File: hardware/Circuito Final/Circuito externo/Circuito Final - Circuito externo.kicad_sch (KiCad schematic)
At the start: 81 parts, among them J1 Conn_02x19_Odd_Even, J2 Conn_02x19_Odd_Even, J3 Conn_01x02, J4 Conn_01x02, J5 Conn_01x03_Pin, Q1 FDMS6681Z, Q2 FDMS6681Z, Q3 MMBT2222A, SW1 SW_SPDT, SW2 SW_DIP_x04, SW3 SW_DIP_x04, SW4 SW_DIP_x01, SW5 SW_DIP_x01, SW6 SW_DIP_x01, U1 Opamp_Quad, U2 ICL7660, U3 INA180A1, U4 INA180A1

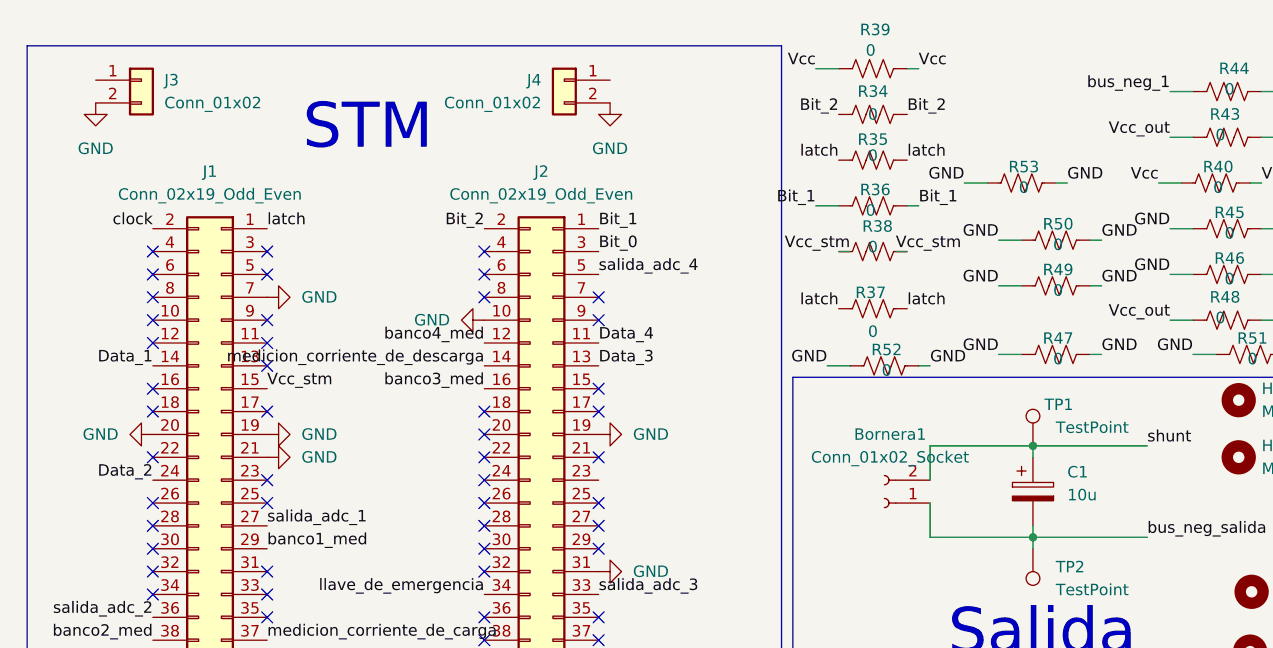
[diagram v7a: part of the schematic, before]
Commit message: sube placa con los oines arreglados
estaba mal data 2, data 1, y vcc
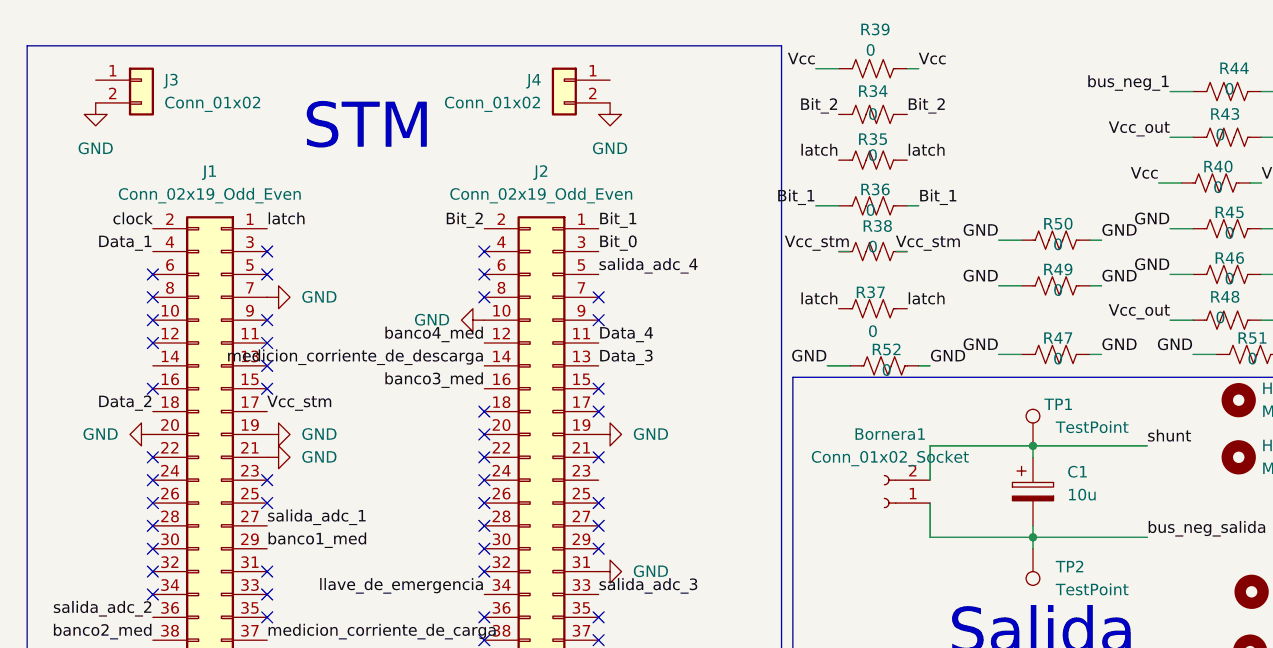
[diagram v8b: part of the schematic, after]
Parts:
- removed R53: 0, Resistor_SMD:R_1206_3216Metric_Pad1.30x1.75mm_HandSolder, symbol Device:R_US
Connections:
- net Data_1: now also J1.4 (Pin_4); no longer J1.14 (Pin_14)
- net Data_2: now also J1.18 (Pin_18); no longer J1.24 (Pin_24)
- net Vcc_stm: now also J1.17 (Pin_17); no longer J1.15 (Pin_15)
- no-connect marks 48 -> 47
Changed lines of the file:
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@@
 	)
 	(no_connect
-		(at 25.4 55.88)
-	)
-	(no_connect
 		(at 38.1 78.74)
 	)
@@
 	)
 	(no_connect
-		(at 25.4 38.1)
-	)
-	(no_connect
 		(at 25.4 60.96)
 	)
@@
 	)
 	(no_connect
-		(at 38.1 55.88)
+		(at 74.93 45.72)
 	)
 	(no_connect
-		(at 74.93 45.72)
+		(at 38.1 53.34)
 	)
 	(no_connect
@@
 	)
 	(no_connect
+		(at 25.4 63.5)
+	)
+	(no_connect
 		(at 25.4 66.04)
 	)
@@
 	(wire
 		(pts
-			(xy 127 30.48) (xy 125.73 30.48)
-		)
-		(stroke
-			(width 0)
-			(type default)
-		)
-	)
-	(wire
-		(pts
 			(xy 251.46 129.54) (xy 251.46 130.81)
 		)
@@
 	(wire
 		(pts
-			(xy 115.57 30.48) (xy 118.11 30.48)
-		)
-		(stroke
-			(width 0)
-			(type default)
-		)
-	)
-	(wire
-		(pts
 			(xy 193.04 34.29) (xy 195.58 34.29)
 		)
@@
 	)
 	(label "GND"
-		(at 127 30.48 0)
-		(effects
-			(font
-				(size 1.27 1.27)
-			)
-			(justify left bottom)
-		)
-	)
-	(label "GND"
 		(at 140.97 49.53 180)
 		(effects
@@
 		)
 	)
-	(label "Data_1"
-		(at 25.4 50.8 180)
+	(label "Data_2"
+		(at 25.4 55.88 180)
 		(effects
 			(font
@@
 	)
 	(label "Vcc_stm"
-		(at 38.1 53.34 0)
+		(at 38.1 55.88 0)
 		(effects
 			(font
@@
 		)
 	)
+	(label "Data_1"
+		(at 25.4 38.1 180)
+		(effects
+			(font
+				(size 1.27 1.27)
+			)
+			(justify right bottom)
+		)
+	)
 	(label "bus_neg_1"
 		(at 180.34 39.37 180)
@@
 		)
 	)
-	(label "GND"
-		(at 115.57 30.48 180)
-		(effects
-			(font
-				(size 1.27 1.27)
-			)
-			(justify right bottom)
-		)
-	)
 	(label "llave_de_emergencia"
 		(at 127 107.95 90)
@@
 		)
 	)
-	(label "Data_2"
-		(at 25.4 63.5 180)
-		(effects
-			(font
-				(size 1.27 1.27)
-			)
-			(justify right bottom)
-		)
-	)
 	(symbol
 		(lib_id "power:GND")
@@
 					(unit 1)
 				)
-			)
-		)
-	)
-	(symbol
-		(lib_id "Device:R_US")
-		(at 121.92 30.48 90)
-		(unit 1)
-		(body_style 1)
-		(exclude_from_sim no)
-		(in_bom yes)
-		(on_board yes)
-		(in_pos_files yes)
-		(dnp no)
-		(property "Reference" "R53"
-			(at 122.174 28.702 90)
-			(show_name no)
-			(do_not_autoplace no)
-			(effects
-				(font
-					(size 1.27 1.27)
-				)
-			)
-		)
-		(property "Value" "0"
-			(at 122.174 30.988 90)
-			(show_name no)
-			(do_not_autoplace no)
-			(effects
-				(font
-					(size 1.27 1.27)
-				)
-			)
-		)
-		(property "Footprint" "Resistor_SMD:R_1206_3216Metric_Pad1.30x1.75mm_HandSolder"
-			(at 122.174 29.464 90)
-			(hide yes)
-			(show_name no)
-			(do_not_autoplace no)
-			(effects
-				(font
-					(size 1.27 1.27)
-				)
-			)
-		)
-		(property "Datasheet" ""
-			(at 121.92 30.48 0)
-			(hide yes)
-			(show_name no)
-			(do_not_autoplace no)
-			(effects
-				(font
-					(size 1.27 1.27)
-				)
-			)
-		)
-		(property "Description" "Resistor, US symbol"
-			(at 121.92 30.48 0)
-			(hide yes)
-			(show_name no)
-			(do_not_autoplace no)
-			(effects
-				(font
-					(size 1.27 1.27)
-				)
-			)
-		)
-		(pin "1"
-		)
-		(pin "2"
-		)
-		(instances
-			(project "Circuito Final - Circuito externo"
-				(path "/f0782466-24b0-4466-90f1-cde2f15c75b0"
-					(reference "R53")
-					(unit 1)
-				)
